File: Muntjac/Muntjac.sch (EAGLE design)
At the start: 106 parts, among them U1 CC2538, U10 DMG6602SVT, U11 SN74AVC4T774PW, U12 TMP102AIDRLT, U2 CC1120_RHM_32, U3 TPD2E001IDRLRQ1, U4 CP2103, U5 BSS138PS, U6 BSS138PS, U7 BSS138PS, U8 M25P16VMN6P, U9 DMG6602SVT, X1 FA-128, X2 32MHz, X3 32.768K

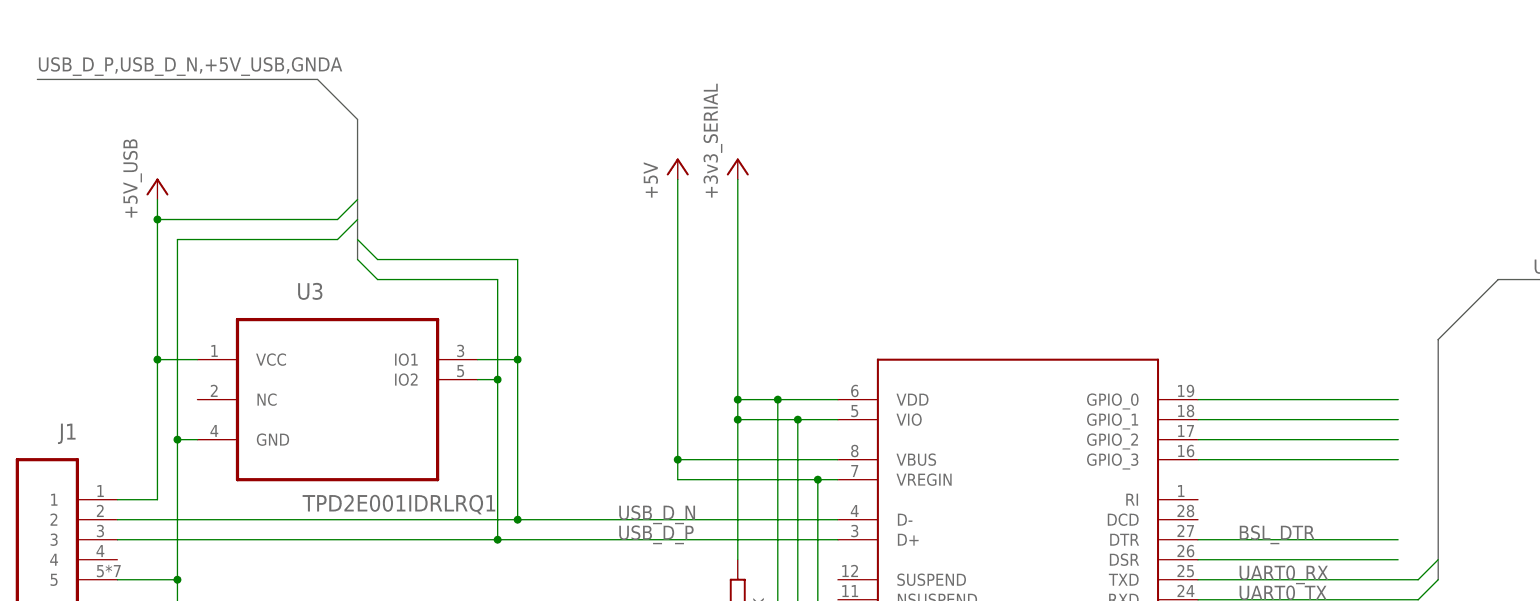
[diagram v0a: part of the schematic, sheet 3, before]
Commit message: Added LEDs for Serial TX/RX.
brd as submitted for manufacture.
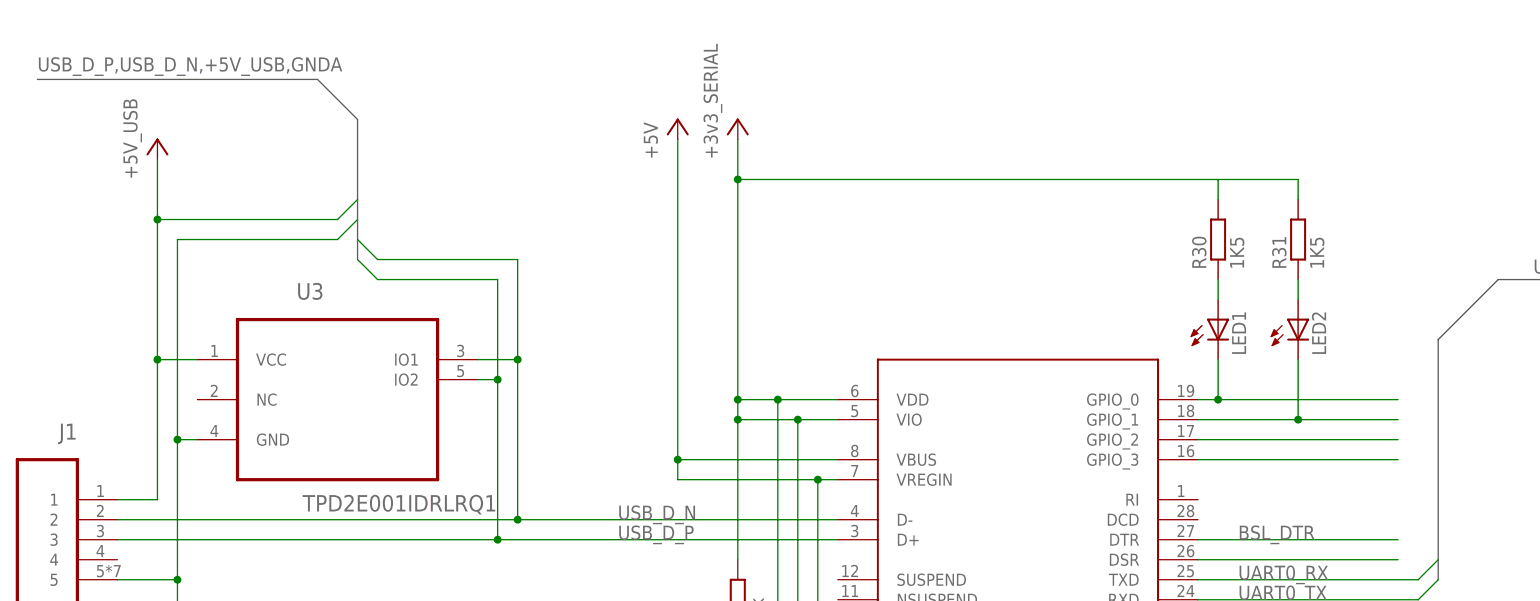
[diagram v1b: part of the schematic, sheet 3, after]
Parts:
- added LED1, LED2: (no value), led:LEDSML0603
- added R30, R31: 1K5, rcl:R-EU_R0603
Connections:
- new net N$20: LED1.A, R30.1
- new net N$40: LED2.A, R31.1
- net +3V3_SERIAL: now also R30.2, R31.2
- net N$15: now also LED1.C
- net N$17: now also LED2.C
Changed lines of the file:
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@@
 <part name="C20" library="CC11x" deviceset="C_EU" device="S" technology="C0603" value="1uF"/>
 <part name="R10" library="rcl" deviceset="R-EU_" device="R0603" value="100k"/>
+<part name="LED1" library="led" deviceset="LED" device="SML0603"/>
+<part name="LED2" library="led" deviceset="LED" device="SML0603"/>
+<part name="R30" library="rcl" deviceset="R-EU_" device="R0603" value="1K5"/>
+<part name="R31" library="rcl" deviceset="R-EU_" device="R0603" value="1K5"/>
 </parts>
 <sheets>
@@
 <instance part="FRAME4" gate="G$1" x="0" y="0"/>
 <instance part="U4" gate="U$1" x="220.98" y="160.02"/>
-<instance part="+3V3_SERIAL" gate="G$1" x="185.42" y="208.28"/>
-<instance part="+5V" gate="1" x="177.8" y="208.28"/>
+<instance part="+3V3_SERIAL" gate="G$1" x="185.42" y="213.36"/>
+<instance part="+5V" gate="1" x="177.8" y="213.36"/>
 <instance part="GND16" gate="1" x="220.98" y="132.08"/>
 <instance part="U3" gate="A" x="134.62" y="180.34"/>
 <instance part="GND7" gate="1" x="114.3" y="134.62"/>
-<instance part="+5V_USB" gate="1" x="111.76" y="205.74"/>
+<instance part="+5V_USB" gate="1" x="111.76" y="210.82"/>
 <instance part="C1" gate="G$1" x="175.26" y="132.08" rot="MR0"/>
 <instance part="C2" gate="G$1" x="203.2" y="129.54" rot="MR180"/>
@@
 <instance part="R27" gate="G$1" x="127" y="38.1" rot="R90"/>
 <instance part="GND23" gate="1" x="137.16" y="25.4"/>
+<instance part="LED1" gate="G$1" x="246.38" y="187.96"/>
+<instance part="LED2" gate="G$1" x="256.54" y="187.96"/>
+<instance part="R30" gate="G$1" x="246.38" y="198.12" rot="R90"/>
+<instance part="R31" gate="G$1" x="256.54" y="198.12" rot="R90"/>
 </instances>
 <busses>
@@
 <wire x1="185.42" y1="177.8" x2="185.42" y2="205.74" width="0.1524" layer="91"/>
 <pinref part="U4" gate="U$1" pin="VIO"/>
+<wire x1="185.42" y1="205.74" x2="185.42" y2="210.82" width="0.1524" layer="91"/>
 <wire x1="198.12" y1="175.26" x2="193.04" y2="175.26" width="0.1524" layer="91"/>
 <wire x1="193.04" y1="175.26" x2="185.42" y2="175.26" width="0.1524" layer="91"/>
@@
 <wire x1="185.42" y1="157.48" x2="185.42" y2="175.26" width="0.1524" layer="91"/>
 <junction x="185.42" y="175.26"/>
+<pinref part="R31" gate="G$1" pin="2"/>
+<wire x1="256.54" y1="203.2" x2="256.54" y2="205.74" width="0.1524" layer="91"/>
+<wire x1="256.54" y1="205.74" x2="246.38" y2="205.74" width="0.1524" layer="91"/>
+<pinref part="R30" gate="G$1" pin="2"/>
+<wire x1="246.38" y1="205.74" x2="246.38" y2="203.2" width="0.1524" layer="91"/>
+<wire x1="246.38" y1="205.74" x2="185.42" y2="205.74" width="0.1524" layer="91"/>
+<junction x="185.42" y="205.74"/>
 </segment>
 </net>
@@
 <pinref part="+5V" gate="1" pin="+5V"/>
 <wire x1="198.12" y1="170.18" x2="177.8" y2="170.18" width="0.1524" layer="91"/>
-<wire x1="177.8" y1="170.18" x2="177.8" y2="205.74" width="0.1524" layer="91"/>
+<wire x1="177.8" y1="170.18" x2="177.8" y2="210.82" width="0.1524" layer="91"/>
 <pinref part="U4" gate="U$1" pin="VREGIN"/>
 <wire x1="198.12" y1="167.64" x2="195.58" y2="167.64" width="0.1524" layer="91"/>
@@
 <wire x1="111.76" y1="182.88" x2="111.76" y2="200.66" width="0.1524" layer="91"/>
 <pinref part="J1" gate="G$1" pin="1"/>
-<wire x1="111.76" y1="200.66" x2="111.76" y2="203.2" width="0.1524" layer="91"/>
+<wire x1="111.76" y1="200.66" x2="111.76" y2="208.28" width="0.1524" layer="91"/>
 <wire x1="106.68" y1="165.1" x2="111.76" y2="165.1" width="0.1524" layer="91"/>
 <wire x1="111.76" y1="165.1" x2="111.76" y2="182.88" width="0.1524" layer="91"/>
@@
 <segment>
 <pinref part="U4" gate="U$1" pin="GPIO_0"/>
-<wire x1="243.84" y1="177.8" x2="269.24" y2="177.8" width="0.1524" layer="91"/>
+<wire x1="243.84" y1="177.8" x2="246.38" y2="177.8" width="0.1524" layer="91"/>
+<pinref part="LED1" gate="G$1" pin="C"/>
+<wire x1="246.38" y1="177.8" x2="269.24" y2="177.8" width="0.1524" layer="91"/>
+<wire x1="246.38" y1="182.88" x2="246.38" y2="177.8" width="0.1524" layer="91"/>
+<junction x="246.38" y="177.8"/>
 </segment>
 </net>
@@
 <segment>
 <pinref part="U4" gate="U$1" pin="GPIO_1"/>
-<wire x1="243.84" y1="175.26" x2="269.24" y2="175.26" width="0.1524" layer="91"/>
+<wire x1="243.84" y1="175.26" x2="256.54" y2="175.26" width="0.1524" layer="91"/>
+<pinref part="LED2" gate="G$1" pin="C"/>
+<wire x1="256.54" y1="175.26" x2="269.24" y2="175.26" width="0.1524" layer="91"/>
+<wire x1="256.54" y1="182.88" x2="256.54" y2="175.26" width="0.1524" layer="91"/>
+<junction x="256.54" y="175.26"/>
 </segment>
 </net>
@@
 </segment>
 </net>
+<net name="N$20" class="0">
+<segment>
+<pinref part="R30" gate="G$1" pin="1"/>
+<pinref part="LED1" gate="G$1" pin="A"/>
+<wire x1="246.38" y1="193.04" x2="246.38" y2="190.5" width="0.1524" layer="91"/>
+</segment>
+</net>
+<net name="N$40" class="0">
+<segment>
+<pinref part="R31" gate="G$1" pin="1"/>
+<pinref part="LED2" gate="G$1" pin="A"/>
+<wire x1="256.54" y1="193.04" x2="256.54" y2="190.5" width="0.1524" layer="91"/>
+</segment>
+</net>

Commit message: Final Muntjac 1.0 commit for manufacture
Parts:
- added C21: 22uF, CC11x:C_EUC0603S
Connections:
- net GND: now also C21.2
- net MEM_VCC: now also C21.1
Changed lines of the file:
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@@
 <part name="R30" library="rcl" deviceset="R-EU_" device="R0603" value="1K5"/>
 <part name="R31" library="rcl" deviceset="R-EU_" device="R0603" value="1K5"/>
+<part name="C21" library="CC11x" deviceset="C_EU" device="S" technology="C0603" value="22uF"/>
 </parts>
 <sheets>
@@
 <instance part="C20" gate="G$1" x="210.82" y="167.64" rot="MR0"/>
 <instance part="R10" gate="G$1" x="198.12" y="190.5" rot="R90"/>
+<instance part="C21" gate="G$1" x="195.58" y="152.4" rot="MR0"/>
 </instances>
 <busses>
@@
 <wire x1="172.72" y1="142.24" x2="172.72" y2="139.7" width="0.1524" layer="91"/>
 <wire x1="172.72" y1="139.7" x2="172.72" y2="137.16" width="0.1524" layer="91"/>
-<wire x1="172.72" y1="139.7" x2="198.12" y2="139.7" width="0.1524" layer="91"/>
+<wire x1="172.72" y1="139.7" x2="195.58" y2="139.7" width="0.1524" layer="91"/>
 <pinref part="SD1" gate="G$1" pin="SWITCH"/>
+<wire x1="195.58" y1="139.7" x2="198.12" y2="139.7" width="0.1524" layer="91"/>
 <wire x1="193.04" y1="167.64" x2="198.12" y2="167.64" width="0.1524" layer="91"/>
 <wire x1="198.12" y1="139.7" x2="198.12" y2="160.02" width="0.1524" layer="91"/>
@@
 <wire x1="210.82" y1="160.02" x2="198.12" y2="160.02" width="0.1524" layer="91"/>
 <junction x="198.12" y="160.02"/>
+<pinref part="C21" gate="G$1" pin="2"/>
+<wire x1="195.58" y1="147.32" x2="195.58" y2="139.7" width="0.1524" layer="91"/>
+<junction x="195.58" y="139.7"/>
 </segment>
 <segment>
@@
 <wire x1="172.72" y1="200.66" x2="172.72" y2="213.36" width="0.1524" layer="91"/>
 <wire x1="198.12" y1="195.58" x2="198.12" y2="200.66" width="0.1524" layer="91"/>
-<wire x1="198.12" y1="200.66" x2="172.72" y2="200.66" width="0.1524" layer="91"/>
+<wire x1="198.12" y1="200.66" x2="195.58" y2="200.66" width="0.1524" layer="91"/>
 <junction x="172.72" y="200.66"/>
-</segment>
-</net>
+<pinref part="C21" gate="G$1" pin="1"/>
+<wire x1="195.58" y1="200.66" x2="172.72" y2="200.66" width="0.1524" layer="91"/>
+<wire x1="195.58" y1="154.94" x2="195.58" y2="200.66" width="0.1524" layer="91"/>
+<junction x="195.58" y="200.66"/>
+</segment>
+</net>

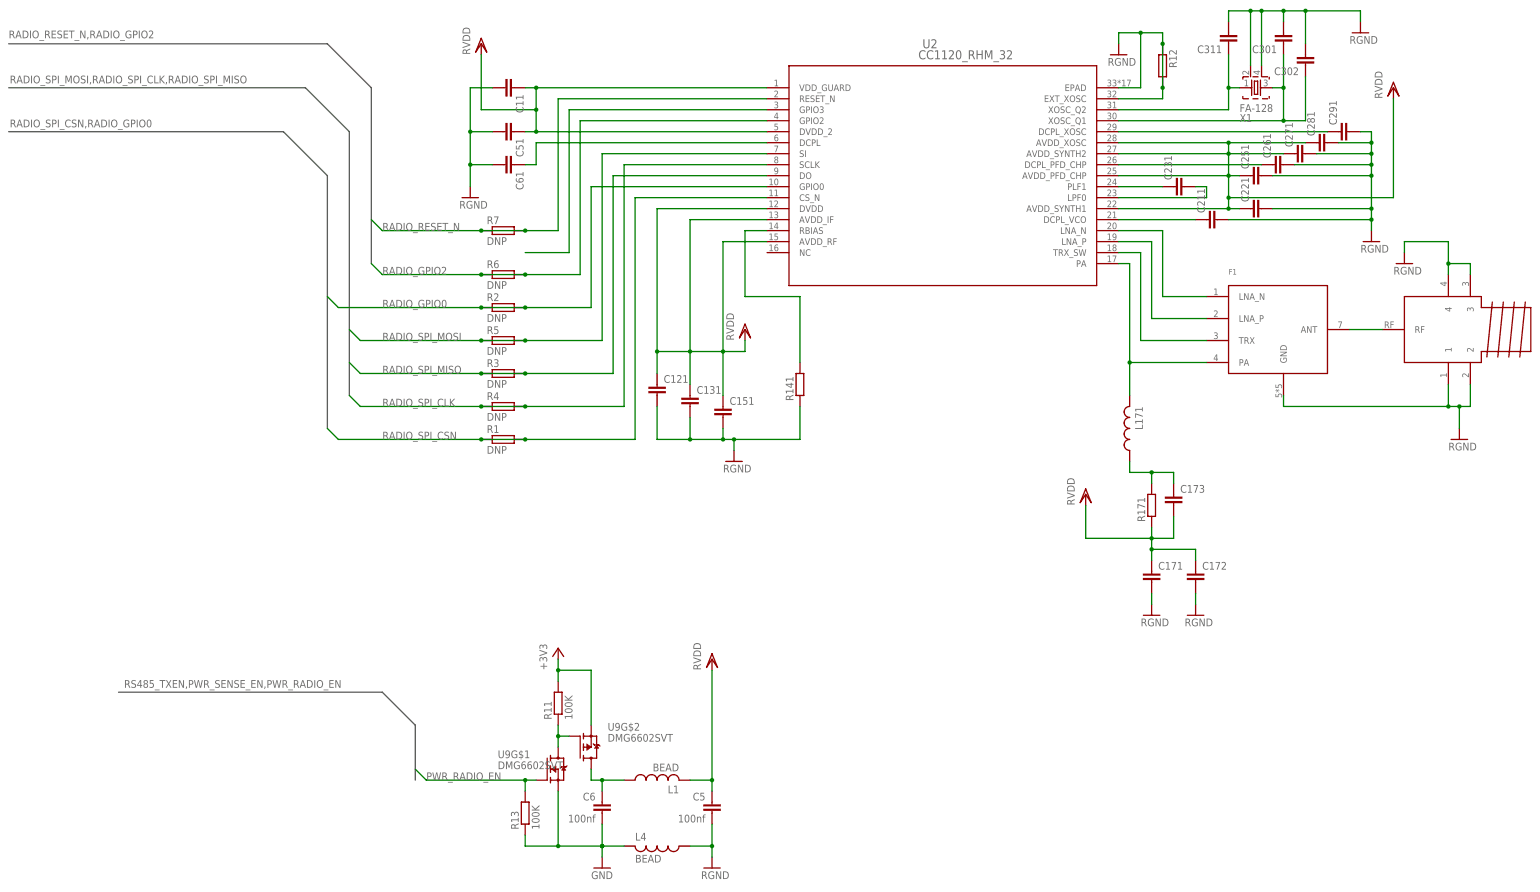
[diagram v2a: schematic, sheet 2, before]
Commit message: Added values to schematic for CC1120 layout.
Updated parts list.
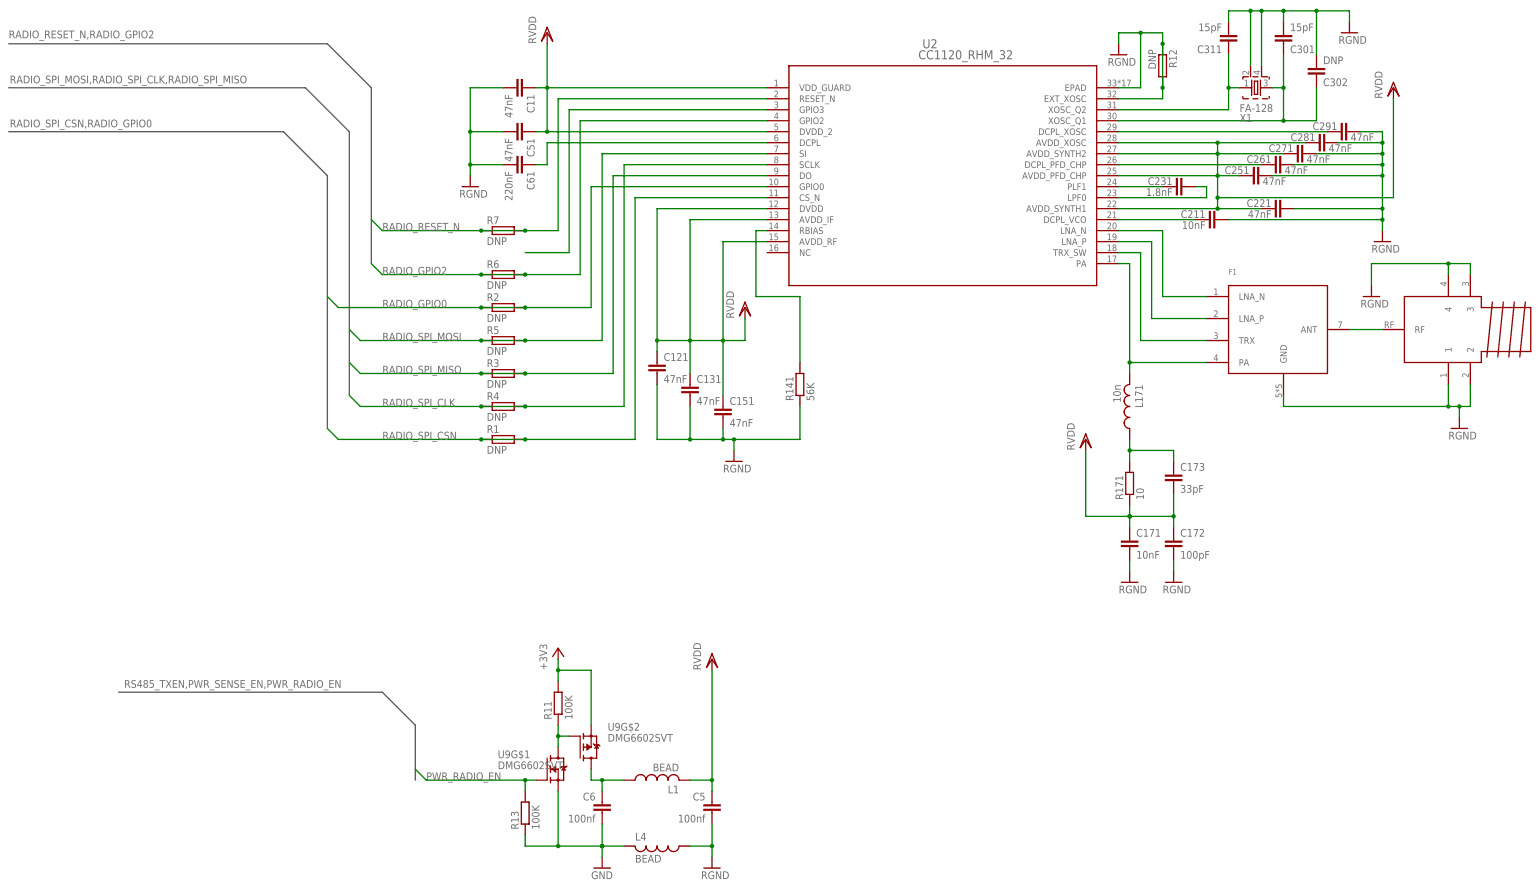
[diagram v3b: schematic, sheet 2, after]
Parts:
- C11, C121, C131, C151, C221, C251, C261, C271, C281, C291, C51: value C_EU0402S -> 47nF
- C171, C211: value C_EU0402S -> 10nF
- C172: value C_EU0402S -> 100pF
- C173: value C_EU0402S -> 33pF
- C231: value C_EU0402S -> 1.8nF
- C301, C311: value C_EU0402S -> 15pF
- C302: value C_EU0402S -> DNP
- C61: value C_EU0402S -> 220nF
- L171: value L_US0402S -> 10n
- R12: value R_EU -> DNP
- R141: value R_EU -> 56K
- R171: value R_EU -> 10
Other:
- moved on the sheet: C11, C121, C131, C171, C172, C173, C20, C21, C221, C302, C51, C61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
